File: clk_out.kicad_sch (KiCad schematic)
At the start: 11 parts, among them U1001 74LVC1G157, U1002 74LVC2G04

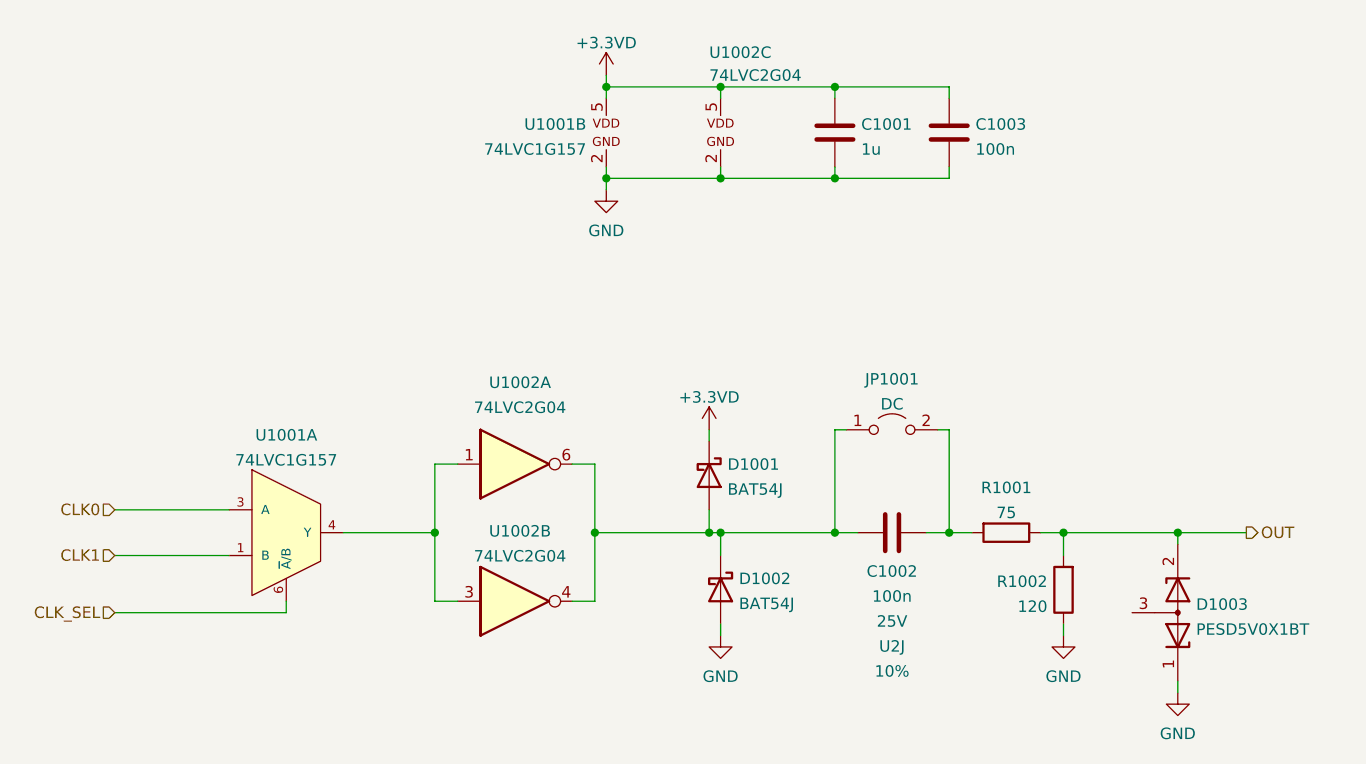
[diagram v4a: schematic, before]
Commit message: Schematic: better LDO output capacitor selection, clarified BOM
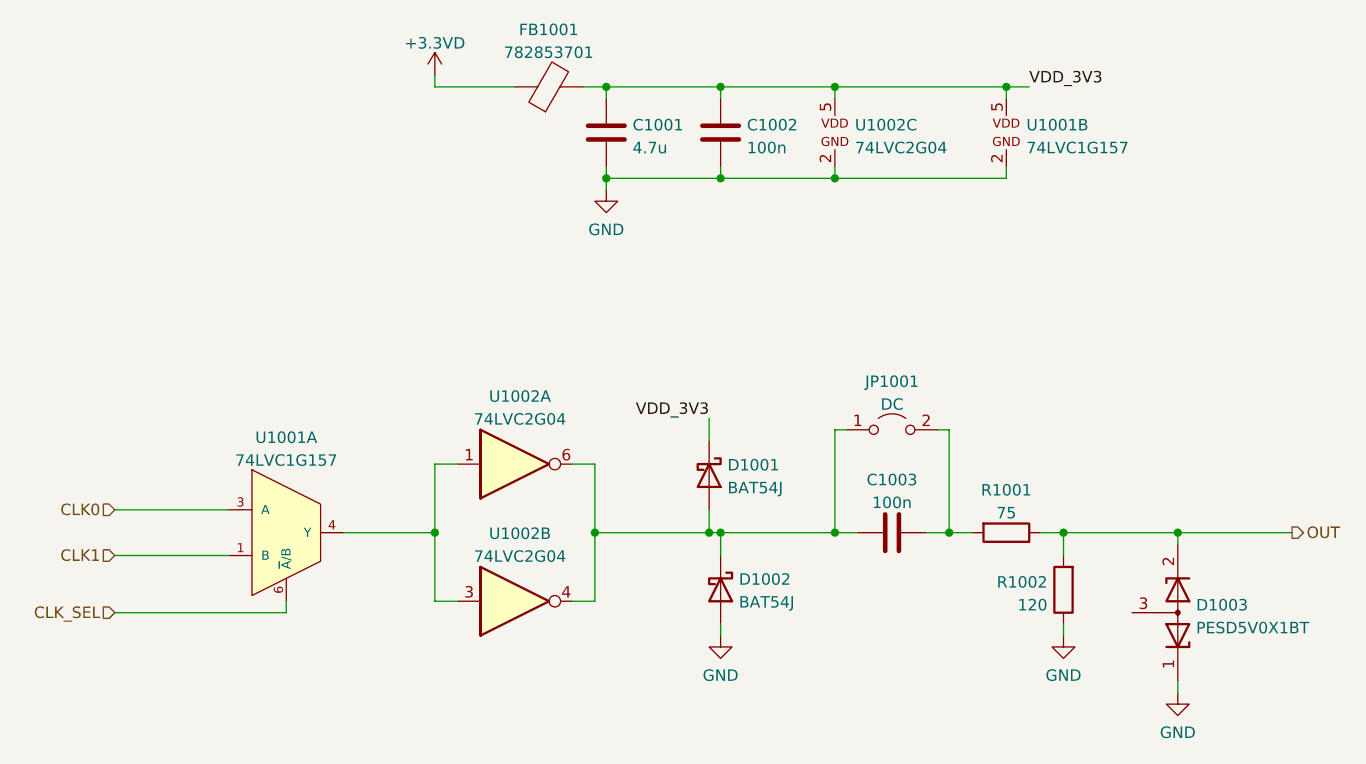
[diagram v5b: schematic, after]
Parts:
- added FB1001: 782853701, Inductor_SMD:L_0805_2012Metric_Pad1.05x1.20mm_HandSolder, symbol Device:FerriteBead
- C1001: value 1u -> 4.7u; Spec1 16V -> (none); Spec2 X5R -> (none); Tolerance 20% -> (none)
- C1002: renamed from C1003; Spec1 16V -> (none); Spec2 X5R -> (none); Tolerance 20% -> (none)
- C1003: renamed from C1002; footprint Capacitor_SMD:C_1206_3216Metric -> Capacitor_SMD:C_0805_2012Metric; Spec1 25V -> (none); Spec2 U2J -> (none); Tolerance 10% -> (none)
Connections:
- net +3.3VD: now also FB1001.1; no longer C1001.2, C1002.2, D1001.1 (K), U1001.5, U1002.5
- new net VDD_3V3: C1001.2, C1002.2, D1001.1 (K), FB1001.2, U1001.5, U1002.5
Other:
- moved on the sheet: C1001, C1002, U1001B, U1002C

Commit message: Schematic: yet another update -Improve way caps are specified once again -Update cap voltages based on ESD simulation -Make anti-aliasing LC filter more practical - with much less inductors -Specify Mfr & MfrPN for almost all components (most from Mouser, some from Digikey)
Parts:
- C1001: Mfr (none) -> Murata; Mfr PN (none) -> GRM21BR71C475ME51
- C1002, C1003: Mfr (none) -> Samsung; Mfr PN (none) -> CL21B104KBFNNNE
- D1001, D1002: footprint Diode_SMD:D_SOD-323F -> Diode_SMD:D_SOD-323_HandSoldering; Mfr (none) -> Nexperia; Mfr PN (none) -> BAT54HGWX
- D1003: Mfr (none) -> Nexperia; Mfr PN (none) -> PESD5V0X1BT,215
- FB1001: Mfr (none) -> Wurth; Mfr PN (none) -> 782853701
- R1001, R1002: Tolerance 5% -> (none)
- U1001: Mfr (none) -> Nexperia; Mfr PN (none) -> 74LVC1G157GV,125
- U1002: Mfr (none) -> Nexperia; Mfr PN (none) -> 74LVC2G04GV-Q100H
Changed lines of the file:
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@@
+      (effects (font (size 1.27 1.27)) hide)
+    )
+    (property "Mfr" "Nexperia" (id 4) (at 184.15 57.15 0)
+      (effects (font (size 1.27 1.27)) hide)
+    )
+    (property "Mfr PN" "74LVC1G157GV,125" (id 5) (at 184.15 57.15 0)
       (effects (font (size 1.27 1.27)) hide)
     )
@@
       (effects (font (size 1.27 1.27)) hide)
     )
-    (property "Tolerance" "5%" (id 4) (at 184.15 101.6 0)
+    (property "Tolerance" "" (id 4) (at 184.15 101.6 0)
       (effects (font (size 1.27 1.27)) hide)
     )
@@
       (effects (font (size 1.27 1.27)) hide)
     )
+    (property "Mfr" "Samsung" (id 7) (at 171.45 101.6 0)
+      (effects (font (size 1.27 1.27)) hide)
+    )
+    (property "Mfr PN" "CL21B104KBFNNNE" (id 8) (at 171.45 101.6 0)
+      (effects (font (size 1.27 1.27)) hide)
+    )
     (pin "1")
     (pin "2")
@@
       (effects (font (size 1.27 1.27)) hide)
     )
+    (property "Mfr" "Wurth" (id 4) (at 133.35 52.07 0)
+      (effects (font (size 1.27 1.27)) hide)
+    )
+    (property "Mfr PN" "782853701" (id 5) (at 133.35 52.07 0)
+      (effects (font (size 1.27 1.27)) hide)
+    )
     (pin "1")
     (pin "2")
@@
       (effects (font (size 1.27 1.27)) hide)
     )
+    (property "Mfr" "Nexperia" (id 4) (at 128.27 93.98 0)
+      (effects (font (size 1.27 1.27)) hide)
+    )
+    (property "Mfr PN" "74LVC2G04GV-Q100H" (id 5) (at 128.27 93.98 0)
+      (effects (font (size 1.27 1.27)) hide)
+    )
     (pin "1")
     (pin "6")
@@
       (effects (font (size 1.27 1.27)) (justify left))
     )
-    (property "Footprint" "Diode_SMD:D_SOD-323F" (id 2) (at 147.955 107.95 0)
+    (property "Footprint" "Diode_SMD:D_SOD-323_HandSoldering" (id 2) (at 147.955 107.95 0)
       (effects (font (size 1.27 1.27)) hide)
     )
@@
       (effects (font (size 1.27 1.27)) hide)
     )
+    (property "Mfr" "Nexperia" (id 4) (at 152.4 107.95 0)
+      (effects (font (size 1.27 1.27)) hide)
+    )
+    (property "Mfr PN" "BAT54HGWX" (id 5) (at 152.4 107.95 0)
+      (effects (font (size 1.27 1.27)) hide)
+    )
     (pin "1")
     (pin "2")
@@
     )
     (property "Datasheet" "~" (id 3) (at 203.2 110.49 0)
+      (effects (font (size 1.27 1.27)) hide)
+    )
+    (property "Mfr" "Nexperia" (id 4) (at 203.2 110.49 0)
+      (effects (font (size 1.27 1.27)) hide)
+    )
+    (property "Mfr PN" "PESD5V0X1BT,215" (id 5) (at 203.2 110.49 0)
       (effects (font (size 1.27 1.27)) hide)
     )
@@
       (effects (font (size 1.27 1.27)) hide)
     )
-    (property "Tolerance" "5%" (id 4) (at 190.5 107.95 0)
+    (property "Tolerance" "" (id 4) (at 190.5 107.95 0)
       (effects (font (size 1.27 1.27)) hide)
     )
@@
       (effects (font (size 1.27 1.27)) (justify left))
     )
-    (property "Footprint" "Diode_SMD:D_SOD-323F" (id 2) (at 146.685 95.25 0)
+    (property "Footprint" "Diode_SMD:D_SOD-323_HandSoldering" (id 2) (at 146.685 95.25 0)
       (effects (font (size 1.27 1.27)) hide)
     )
     (property "Datasheet" "https://assets.nexperia.com/documents/data-sheet/BAT54J.pdf" (id 3) (at 151.13 95.25 0)
+      (effects (font (size 1.27 1.27)) hide)
+    )
+    (property "Mfr" "Nexperia" (id 4) (at 151.13 95.25 0)
+      (effects (font (size 1.27 1.27)) hide)
+    )
+    (property "Mfr PN" "BAT54HGWX" (id 5) (at 151.13 95.25 0)
       (effects (font (size 1.27 1.27)) hide)
     )
@@
       (effects (font (size 1.27 1.27)) hide)
     )
+    (property "Mfr" "Samsung" (id 7) (at 152.4 57.15 0)
+      (effects (font (size 1.27 1.27)) hide)
+    )
+    (property "Mfr PN" "CL21B104KBFNNNE" (id 8) (at 152.4 57.15 0)
+      (effects (font (size 1.27 1.27)) hide)
+    )
     (pin "1")
     (pin "2")
@@
     )
     (property "Datasheet" "https://assets.nexperia.com/documents/data-sheet/74LVC2GU04.pdf" (id 3) (at 163.83 36.83 0)
+      (effects (font (size 1.27 1.27)) hide)
+    )
+    (property "Mfr" "Nexperia" (id 4) (at 165.1 57.15 0)
+      (effects (font (size 1.27 1.27)) hide)
+    )
+    (property "Mfr PN" "74LVC2G04GV-Q100H" (id 5) (at 165.1 57.15 0)
       (effects (font (size 1.27 1.27)) hide)
     )
@@
       (effects (font (size 1.27 1.27)) hide)
     )
+    (property "Mfr" "Nexperia" (id 4) (at 104.14 101.6 0)
+      (effects (font (size 1.27 1.27)) hide)
+    )
+    (property "Mfr PN" "74LVC1G157GV,125" (id 5) (at 104.14 101.6 0)
+      (effects (font (size 1.27 1.27)) hide)
+    )
     (pin "1")
     (pin "3")
@@
       (effects (font (size 1.27 1.27)) hide)
     )
+    (property "Mfr" "Murata" (id 7) (at 139.7 57.15 0)
+      (effects (font (size 1.27 1.27)) hide)
+    )
+    (property "Mfr PN" "GRM21BR71C475ME51" (id 8) (at 139.7 57.15 0)
+      (effects (font (size 1.27 1.27)) hide)
+    )
     (pin "1")
     (pin "2")
@@
       (effects (font (size 1.27 1.27)) hide)
     )
+    (property "Mfr" "Nexperia" (id 4) (at 128.27 109.22 0)
+      (effects (font (size 1.27 1.27)) hide)
+    )
+    (property "Mfr PN" "74LVC2G04GV-Q100H" (id 5) (at 128.27 109.22 0)
+      (effects (font (size 1.27 1.27)) hide)
+    )

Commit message: Schematic: add PNs for resistors
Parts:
- R1001: Mfr (none) -> Bourns; Mfr PN (none) -> CR0805-FX-75R0ELF
- R1002: Mfr (none) -> Bourns; Mfr PN (none) -> CR0805-FX-1200ELF
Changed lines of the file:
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@@
+      (effects (font (size 1.27 1.27)) hide)
+    )
+    (property "Mfr" "Bourns" (id 5) (at 184.15 101.6 0)
+      (effects (font (size 1.27 1.27)) hide)
+    )
+    (property "Mfr PN" "CR0805-FX-75R0ELF" (id 6) (at 184.15 101.6 0)
       (effects (font (size 1.27 1.27)) hide)
     )
@@
       (effects (font (size 1.27 1.27)) hide)
     )
+    (property "Mfr" "Bourns" (id 5) (at 190.5 107.95 0)
+      (effects (font (size 1.27 1.27)) hide)
+    )
+    (property "Mfr PN" "CR0805-FX-1200ELF" (id 6) (at 190.5 107.95 0)
+      (effects (font (size 1.27 1.27)) hide)
+    )
